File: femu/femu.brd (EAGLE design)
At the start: 20 x 15.5 mm, 47 parts, among them IC1 ESP32-QFN_5X5, IC3 FT230XQ, U1 LP5900TL-3.0/NOPB

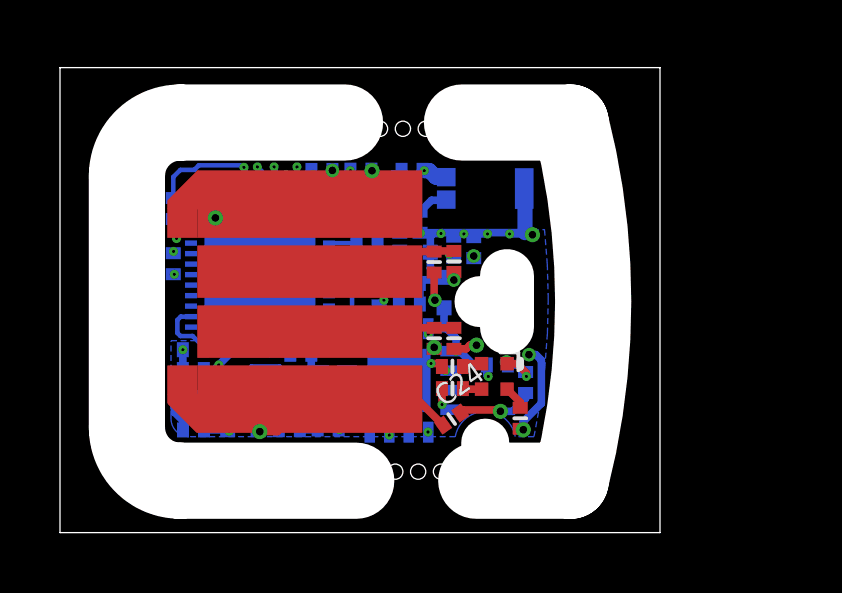
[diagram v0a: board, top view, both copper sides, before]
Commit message: Adding fiducials and stencil jig holes, adjusting dimension labels
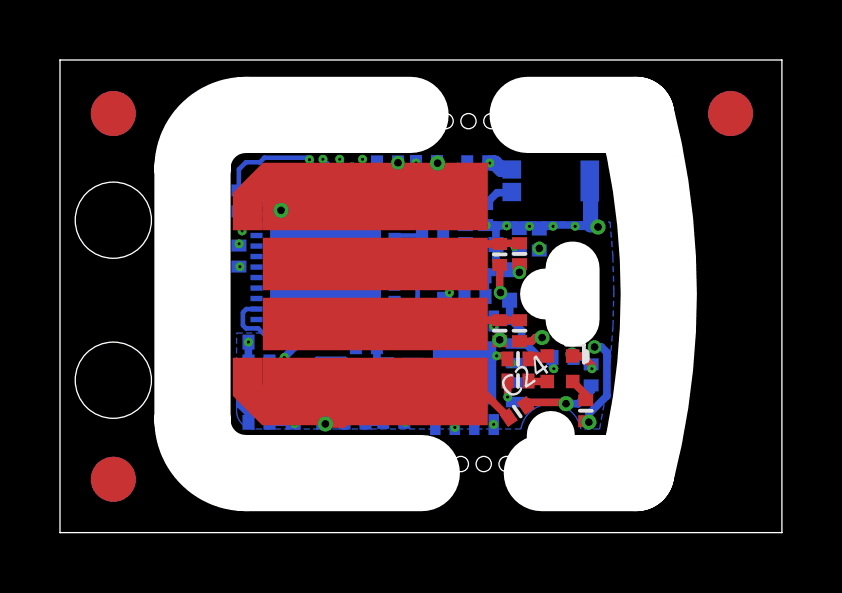
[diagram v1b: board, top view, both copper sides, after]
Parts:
- added FID1, FID2, FID3, FID4, FID5, FID6: FIDUCIAL, adafruit:FIDUCIAL_1MM
- moved FRAME2 5.44 mm to (4.75, 2.93)
- moved FRAME3 4.32 mm to (3.71, 2.66)
- moved FRAME1 2.89 mm to (3.72, 3.32)
- moved C22 2.20 mm to (17.7, 5.26)
- moved L2 2.20 mm to (13.9, 12.3)
- moved R8 2.20 mm to (14.7, 6.73)
- moved R9 2.20 mm to (14.7, 9.27)
- moved RGB1 2.20 mm to (16.7, 5.46)
- moved C1 2.20 mm to (15.3, 9.77)
- moved C10 2.20 mm to (15.0, 8.26)
- moved C11 2.20 mm to (14.0, 9.60)
- moved C12 2.20 mm to (12.5, 11.0)
- moved C13 2.20 mm to (12.2, 12.3)
- moved C15 2.20 mm to (13.8, 8.56)
- moved C16 2.20 mm to (13.8, 7.87)
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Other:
- board size 20 x 15.5 mm -> 24.1 x 15.8 mm

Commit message: Let's try the on semiconductor LDO. Might swap out with something else depending on community guidance regarding heat dissipation. Added edge connectors
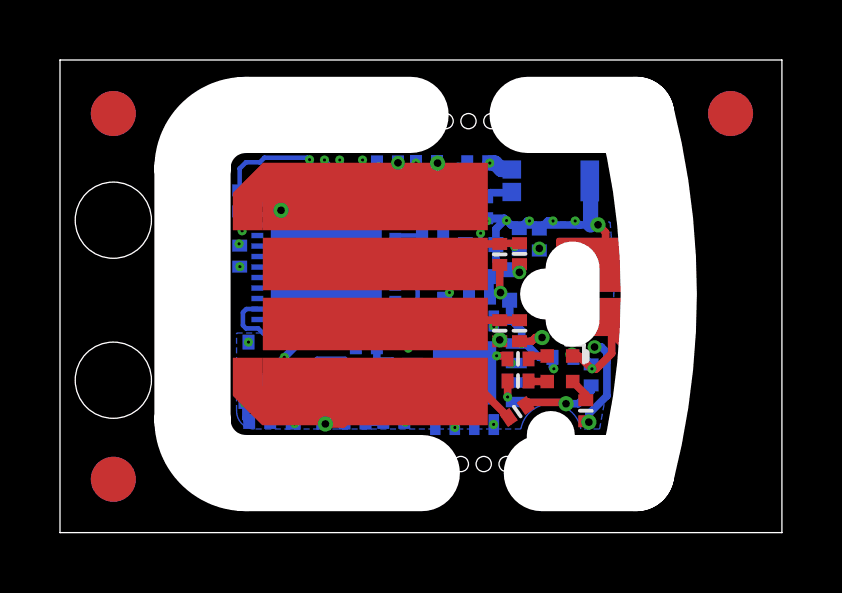
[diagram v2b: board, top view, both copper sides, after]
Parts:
- removed U1: LP5900TL-3.0/NOPB, ti-ldo-3.3v-LP5900TL-3.0__NOPB:TLA04BCA
- added U$33: NCP167AFCT330T2G, onsemi:WLCSP4
- added U$6: FEMU-EDGE-CONNECTOR, femu-edge-connectors:FEMU-EDGE-CONNECTOR
- C2, C3: value 0.47uF -> 1uF
- moved C3 1.10 mm to (6.20, 4.67), turned to 90 degrees
- moved C9 0.23 mm to (14.2, 10.8)
- moved C15 0.18 mm to (14.0, 8.53)
- moved C16 0.15 mm to (14.0, 7.85)
- moved R6 0.15 mm to (13.5, 10.8)
- turned C2 to 180 degrees
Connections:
- removed net IO25: IC1.14
- new net IO25/DAC1: IC1.14, U$6.3
- net 3.3V: now also C3.2, U$33.A2, U$6.2; no longer C3.1, U1.B2
- net GND: now also C2.1, C3.1, U$33.B2, U$6.1; no longer C2.2, C3.2, U1.B1
- net VIN: now also C2.2, U$33.A1, U$33.B1; no longer C2.1, U1.A1, U1.A2
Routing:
- net IO25/DAC1: track 0.00 -> 15.3 mm, vias 0 -> 6
- net 3.3V: track 60.7 -> 62.9 mm
- net GND: track 70.9 -> 71.7 mm, vias 25 -> 26
- net B: track 13.9 -> 14.5 mm
